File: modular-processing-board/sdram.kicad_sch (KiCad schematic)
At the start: 18 parts, among them U301 W9825G6KH-6, U302 W9825G6KH-6

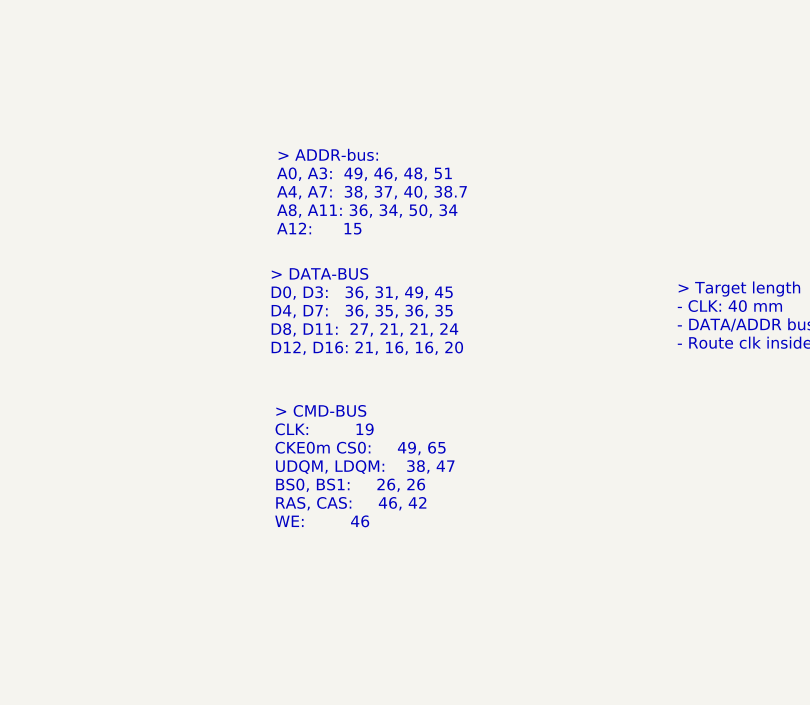
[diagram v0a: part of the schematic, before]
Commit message: rough length mamatching for sdram (next) route PSSI-bus
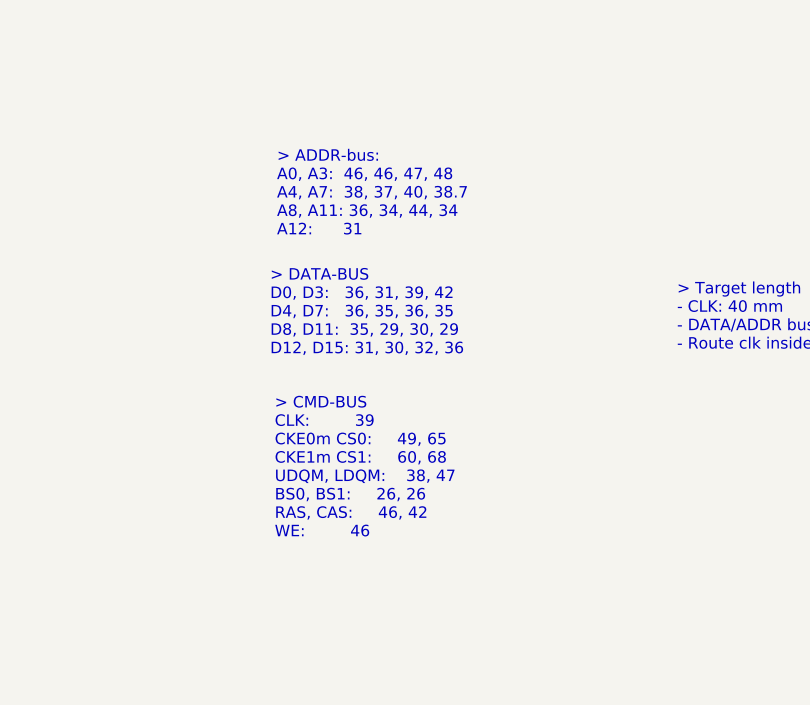
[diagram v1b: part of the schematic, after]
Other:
- note added: "> ADDR-bus: A0, A3: 46, 46, 47, 48 A4, A7: 38, 37, 40, 38.7 A8, A11: 36, 34, 44, 34 A12: 31"
- note added: "> CMD-BUS CLK: 39 CKE0m CS0: 49, 65 CKE1m CS1: 60, 68 UDQM, LDQM: 38, 47 BS0, BS1: 26, 26 RAS, CAS: 46, 42 WE: 46"
- note added: "> DATA-BUS D0, D3: 36, 31, 39, 42 D4, D7: 36, 35, 36, 35 D8, D11: 35, 29, 30, 29 D12, D15: 31, 30, 32, 36"
- note removed: "> ADDR-bus: A0, A3: 49, 46, 48, 51 A4, A7: 38, 37, 40, 38.7 A8, A11: 36, 34, 50, 34 A12: 15"
- note removed: "> CMD-BUS CLK: 19 CKE0m CS0: 49, 65 UDQM, LDQM: 38, 47 BS0, BS1: 26, 26 RAS, CAS: 46, 42 WE: 46"
- note removed: "> DATA-BUS D0, D3: 36, 31, 49, 45 D4, D7: 36, 35, 36, 35 D8, D11: 27, 21, 21, 24 D12, D16: 21, 16, 16, 20"
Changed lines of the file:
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@@
 		)
 	)
-	(text "> DATA-BUS\nD0, D3:   36, 31, 49, 45\nD4, D7:   36, 35, 36, 35\nD8, D11:  27, 21, 21, 24\nD12, D16: 21, 16, 16, 20\n"
+	(text "> DATA-BUS\nD0, D3:   36, 31, 39, 42\nD4, D7:   36, 35, 36, 35\nD8, D11:  35, 29, 30, 29\nD12, D15: 31, 30, 32, 36"
 		(exclude_from_sim no)
 		(at 308.61 86.868 0)
@@
 		)
 	)
-	(text "> CMD-BUS\nCLK: 		19\nCKE0m CS0: 	49, 65\nUDQM, LDQM:	38, 47\nBS0, BS1: 	26, 26\nRAS, CAS: 	46, 42\nWE: 		46"
+	(text "> CMD-BUS\nCLK: 		39\nCKE0m CS0: 	49, 65\nCKE1m CS1: 	60, 68\nUDQM, LDQM:	38, 47\nBS0, BS1: 	26, 26\nRAS, CAS: 	46, 42\nWE: 		46"
 		(exclude_from_sim no)
 		(at 309.118 104.14 0)
@@
 		)
 	)
-	(text "> ADDR-bus:\nA0, A3:  49, 46, 48, 51\nA4, A7:  38, 37, 40, 38.7\nA8, A11: 36, 34, 50, 34\nA12: 	 15\n"
+	(text "> ADDR-bus:\nA0, A3:  46, 46, 47, 48\nA4, A7:  38, 37, 40, 38.7\nA8, A11: 36, 34, 44, 34\nA12: 	 31\n"
 		(exclude_from_sim no)
 		(at 309.372 73.66 0)

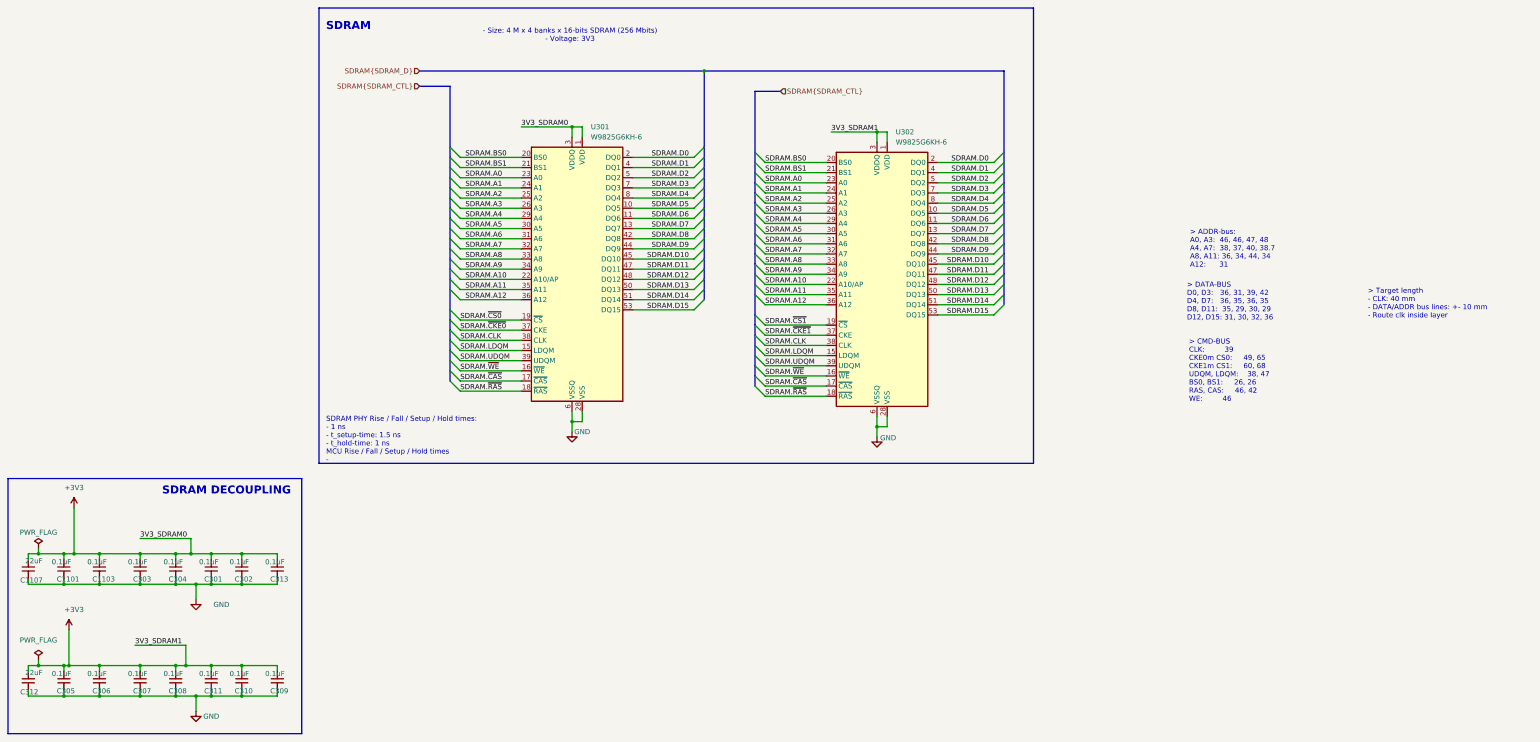
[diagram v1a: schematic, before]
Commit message: replaced sdmmc connector, added smmc trace, added u.fl. connectors
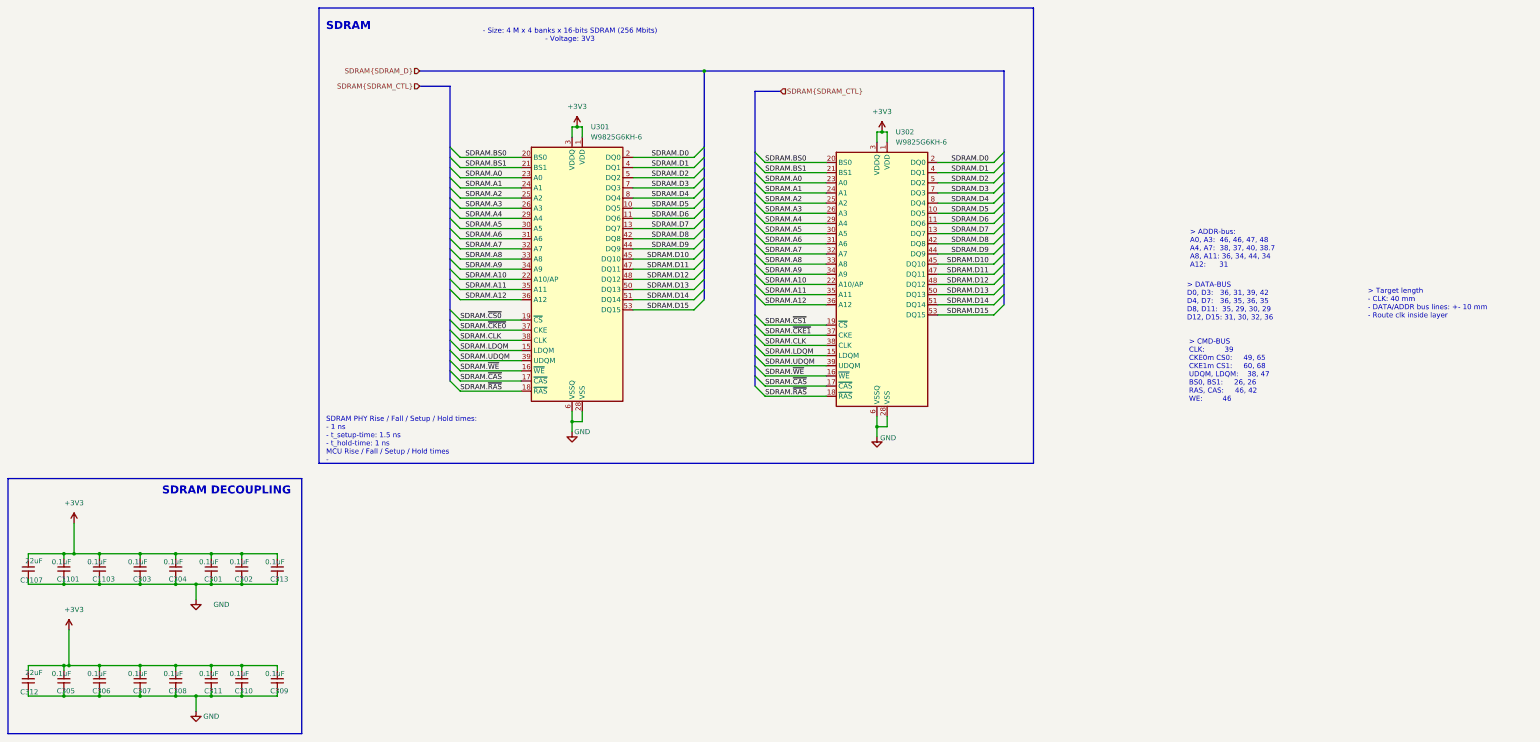
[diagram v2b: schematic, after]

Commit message: checked components part numbers (next) board checks
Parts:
- C1107, C312: LPN (none) -> C59461; MPN (none) -> CL10A226MQ8NRNC
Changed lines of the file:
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@@
+			)
+		)
+		(property "LPN" "C59461"
+			(at 19.05 181.61 0)
+			(effects
+				(font
+					(size 1.27 1.27)
+				)
+				(hide yes)
+			)
+		)
+		(property "MPN" "CL10A226MQ8NRNC"
+			(at 19.05 181.61 0)
+			(effects
+				(font
+					(size 1.27 1.27)
+				)
+				(hide yes)
 			)
 		)
@@
 			(at 19.05 153.67 0)
 			(effects
+				(font
+					(size 1.27 1.27)
+				)
+				(hide yes)
+			)
+		)
+		(property "LPN" "C59461"
+			(at 19.05 153.67 0)
+			(effects
+				(font
+					(size 1.27 1.27)
+				)
+				(hide yes)
+			)
+		)
+		(property "MPN" "CL10A226MQ8NRNC"
+			(at 19.05 153.67 0)
+			(effects

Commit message: matched PSSI bus lenghts
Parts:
- C1101, C1103, C301, C302, C303, C304, C305, C306, C307, C308, C309, C310, C311, C313: LCSC Part Number C22435929 -> (none); Manufacturing Part Number CGA0201X7R104K160ET -> (none)
- C1107, C312: LCSC Part Number C59461 -> (none); Manufacturing Part Number CL10A226MQ8NRNC -> (none)

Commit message: minor change in fw
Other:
- note added: "SDRAM PHY Rise / Fall / Setup / Hold times: - 1 ns - t_setup-time: 1.5 ns - t_hold-time: 1 ns MCU Rise / Fall / Setup / Hold times"
- note removed: "SDRAM PHY Rise / Fall / Setup / Hold times: - 1 ns - t_setup-time: 1.5 ns - t_hold-time: 1 ns MCU Rise / Fall / Setup / Hold times -"
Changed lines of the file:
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@@
 		)
 	)
-	(text "SDRAM PHY Rise / Fall / Setup / Hold times:\n- 1 ns\n- t_setup-time: 1.5 ns\n- t_hold-time: 1 ns\nMCU Rise / Fall / Setup / Hold times\n- "
+	(text "SDRAM PHY Rise / Fall / Setup / Hold times:\n- 1 ns\n- t_setup-time: 1.5 ns\n- t_hold-time: 1 ns\nMCU Rise / Fall / Setup / Hold times"
 		(exclude_from_sim no)
 		(at 93.472 121.412 0)
